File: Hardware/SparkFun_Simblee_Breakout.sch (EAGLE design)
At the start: 18 parts, among them U1 ADP160, U2 RFD77101

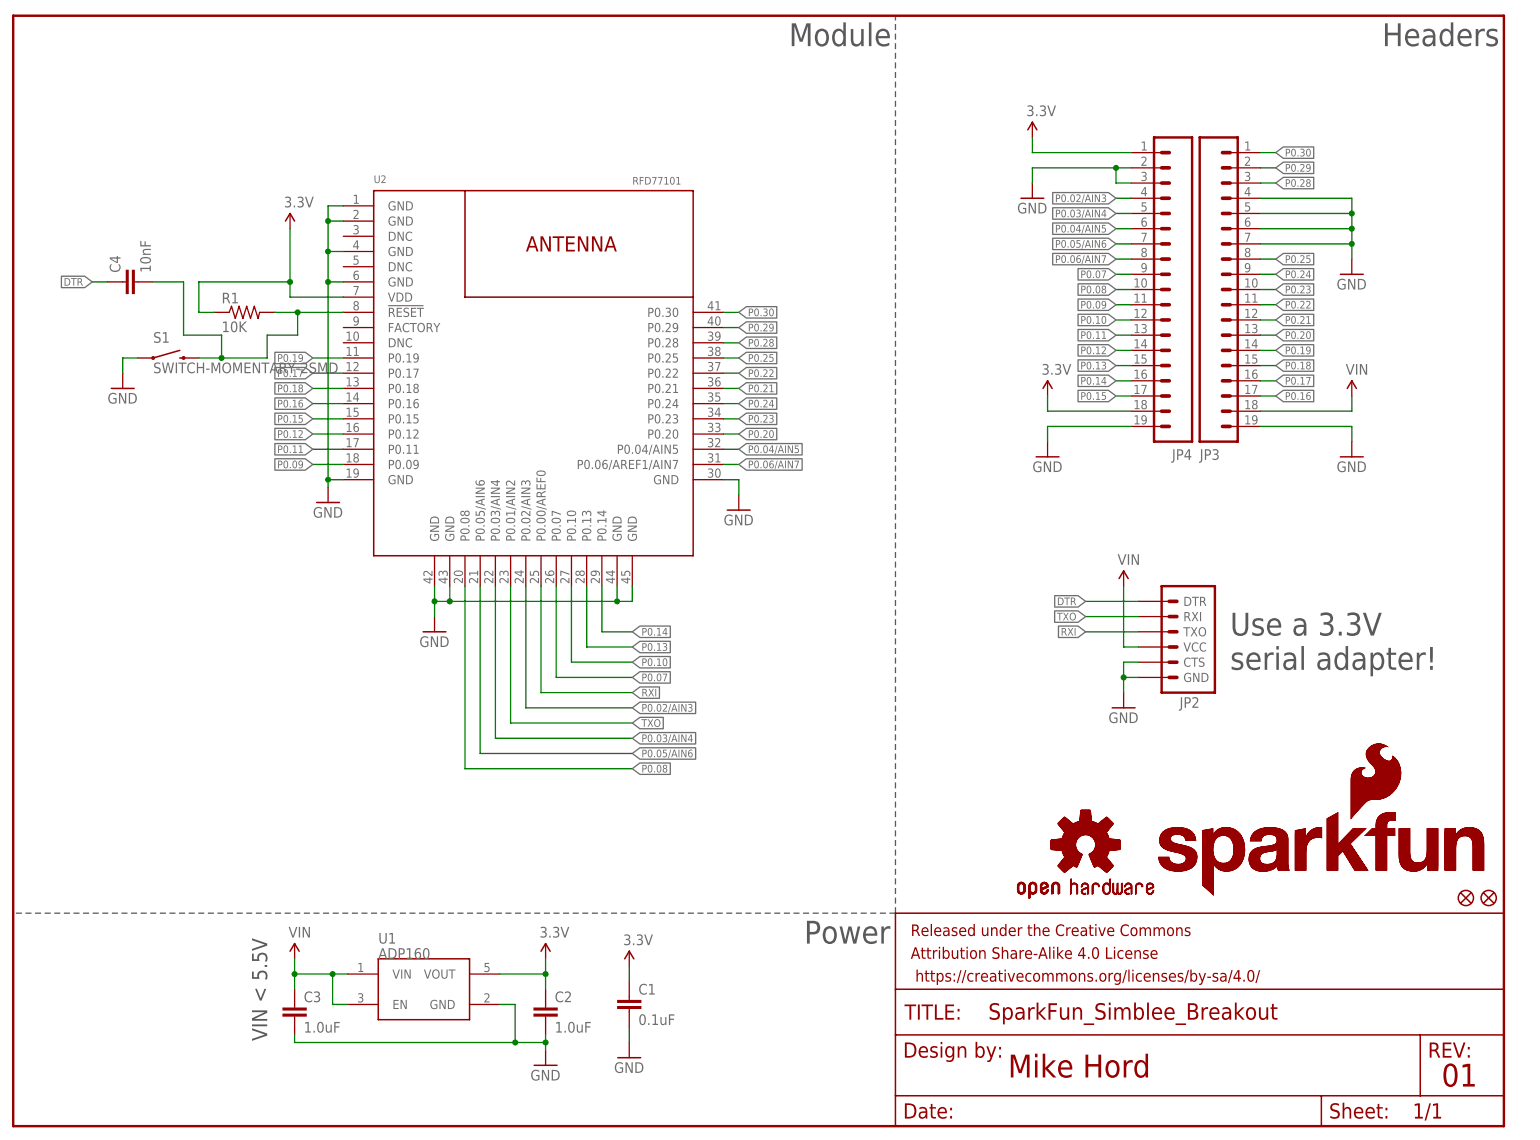
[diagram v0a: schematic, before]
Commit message: Major changes to make compatible with RFDigital stuff
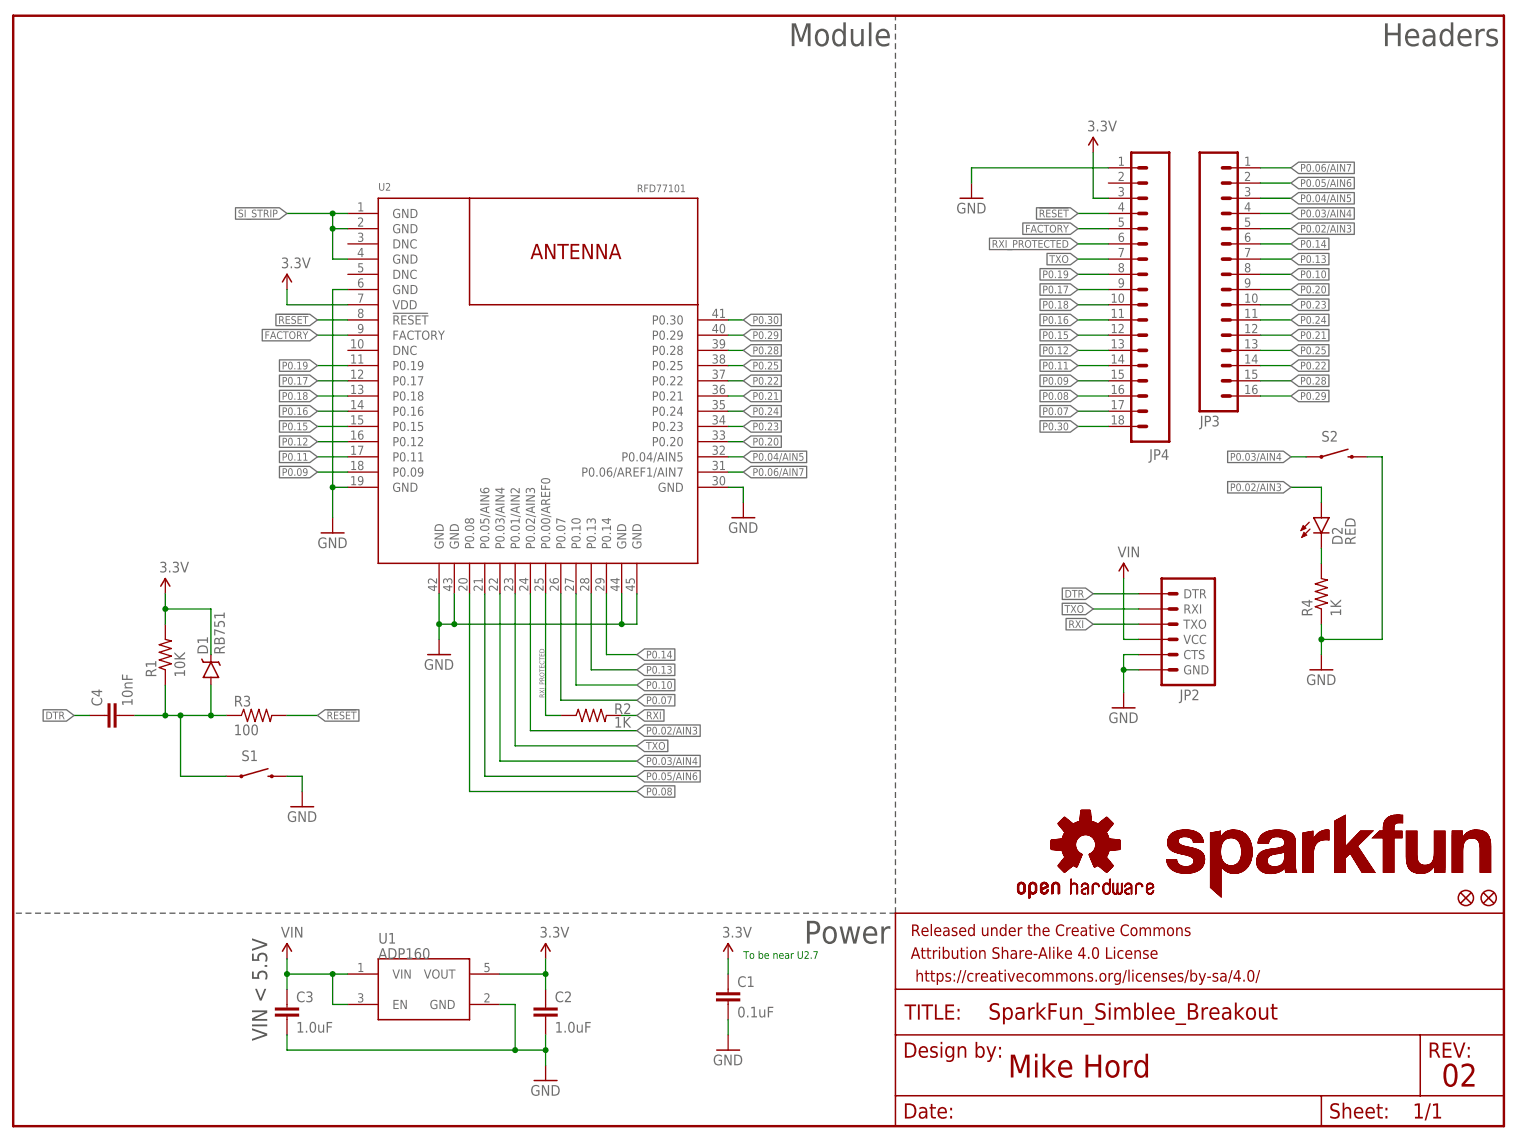
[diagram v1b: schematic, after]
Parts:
- added D1: RB751, SparkFun-DiscreteSemi:DIODE-SCHOTTKY-RB751
- added D2: RED, SparkFun-LED:LED-RED0603
- added R2, R4: 1K, SparkFun-Resistors:1KOHM-1/10W-1%(0603)
- added R3: 100, SparkFun-Resistors:100OHM-1/10W-1%(0603)
- added S2: SWITCH-MOMENTARY-2SMD, SparkFun-Electromechanical:SWITCH-MOMENTARY-2SMD
- JP3: device SparkFun-Connectors:M191X19 -> SparkFun-Connectors:M16PTH
- JP4: device SparkFun-Connectors:M191X19 -> SparkFun-Connectors:M18_
- LOGO1, LOGO3: value SFE_LOGO_NAME_FLAME.1_INCH -> SFE_LOGO_NAME.1_INCH; device SparkFun-Aesthetics:SFE_LOGO_NAME_FLAME.1_INCH -> SparkFun-Aesthetics:SFE_LOGO_NAME.1_INCH
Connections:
- new net !RESET: JP4.4, R3.2, U2.!RESET!
- new net FACTORY: JP4.5, U2.FACTORY
- new net N$2: D2.C, R4.2
- new net RXI_PROTECTED: JP4.6, R2.1, U2.P0.00/AREF0
- new net SI_STRIP: U2.GND@1, U2.GND@2, U2.GND@4
- net 3.3V: now also D1.C, JP4.3, R1.2; no longer JP4.1, JP4.18, R1.1
- net GND: now also JP4.1, R4.1, S1.2, S2.2; no longer JP3.19, JP3.4, JP3.5, JP3.6, JP3.7, JP4.19, JP4.2, JP4.3, S1.1, U2.GND@1, U2.GND@2, U2.GND@4
- net N$1: now also D1.A, R1.1, R3.1, S1.1; no longer R1.2, S1.2, U2.!RESET!
- net P0.02/AIN3: now also D2.A, JP3.5; no longer JP4.4
- net P0.03/AIN4: now also JP3.4, S2.1; no longer JP4.5
- net P0.04/AIN5: now also JP3.3; no longer JP4.6
- net P0.05/AIN6: now also JP3.2; no longer JP4.7
- net P0.06/AIN7: now also JP3.1; no longer JP4.8
- net P0.07: now also JP4.17; no longer JP4.9
- net P0.08: now also JP4.16; no longer JP4.10
- net P0.09: now also JP4.15; no longer JP4.11
- net P0.10: now also JP3.8; no longer JP4.12
- net P0.11: now also JP4.14; no longer JP4.13
- net P0.12: now also JP4.13; no longer JP4.14
- net P0.13: now also JP3.7; no longer JP4.15
- net P0.14: now also JP3.6; no longer JP4.16
- net P0.15: now also JP4.12; no longer JP4.17
- net P0.16: now also JP4.11; no longer JP3.17
- net P0.17: now also JP4.9; no longer JP3.16
- net P0.18: now also JP4.10; no longer JP3.15
- net P0.19: now also JP4.8; no longer JP3.14
- net P0.20: now also JP3.9; no longer JP3.13
- net P0.22: now also JP3.14; no longer JP3.11
- net P0.24: now also JP3.11; no longer JP3.9
- net P0.25: now also JP3.13; no longer JP3.8
- net P0.28: now also JP3.15; no longer JP3.3
- net P0.29: now also JP3.16; no longer JP3.2
- net P0.30: now also JP4.18; no longer JP3.1
- net RXI: now also R2.2; no longer U2.P0.00/AREF0
- net TXO: now also JP4.7
- net VIN: no longer JP3.18
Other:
- note added: "02"
- note added: "To be near U2.7"
- note removed: "01"
- note removed: "Use a 3.3V serial adapter!"
- moved on the sheet: C1, C3, C4, JP2, R1, S1, U2

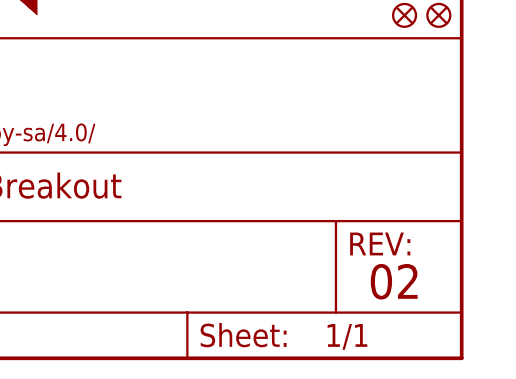
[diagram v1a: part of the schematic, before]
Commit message: Update to v10. Chg gnd pad to 12.5% paste
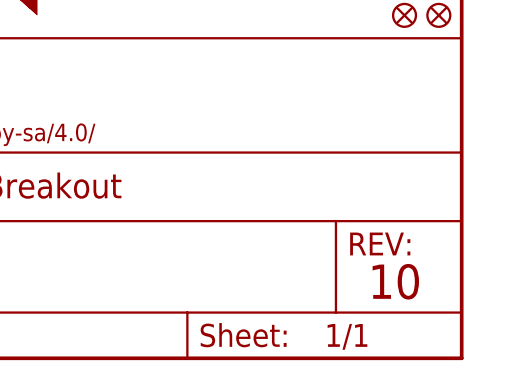
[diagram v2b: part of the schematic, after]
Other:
- note added: "10"
- note removed: "02"
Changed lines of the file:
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@@
 <plain>
 <text x="166.116" y="8.128" size="3.81" layer="94">Mike Hord</text>
-<text x="238.506" y="6.604" size="3.81" layer="94">02</text>
+<text x="238.506" y="6.604" size="3.81" layer="94">10</text>
 <text x="42.418" y="14.224" size="2.54" layer="97" rot="R90">VIN &lt; 5.5V</text>
 <wire x1="147.32" y1="35.56" x2="0" y2="35.56" width="0.1524" layer="97" style="shortdash"/>

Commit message: Rotate SF logo on bottom, ver to 11
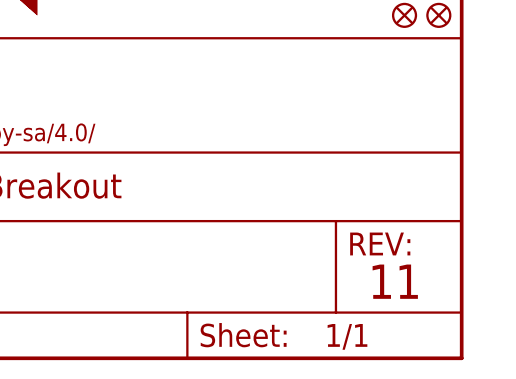
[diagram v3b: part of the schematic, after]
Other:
- note added: "11"
- note removed: "10"
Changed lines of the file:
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@@
 <plain>
 <text x="166.116" y="8.128" size="3.81" layer="94">Mike Hord</text>
-<text x="238.506" y="6.604" size="3.81" layer="94">10</text>
+<text x="238.506" y="6.604" size="3.81" layer="94">11</text>
 <text x="42.418" y="14.224" size="2.54" layer="97" rot="R90">VIN &lt; 5.5V</text>
 <wire x1="147.32" y1="35.56" x2="0" y2="35.56" width="0.1524" layer="97" style="shortdash"/>
